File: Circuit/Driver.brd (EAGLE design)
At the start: 84.6 x 65.2 mm, 33 parts

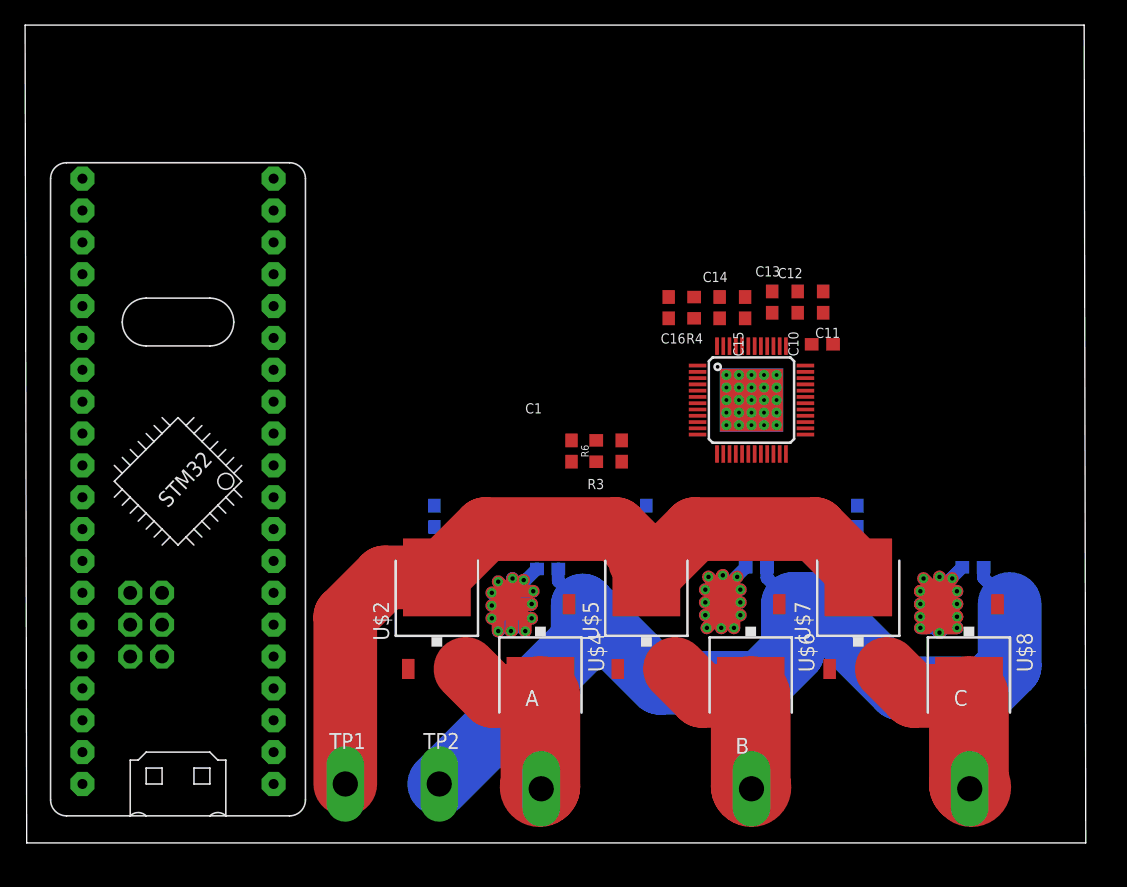
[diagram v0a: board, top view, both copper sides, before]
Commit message: enlarged the width of the vin and added a T-stop wire for large current signal (mosfet GND and VCC)
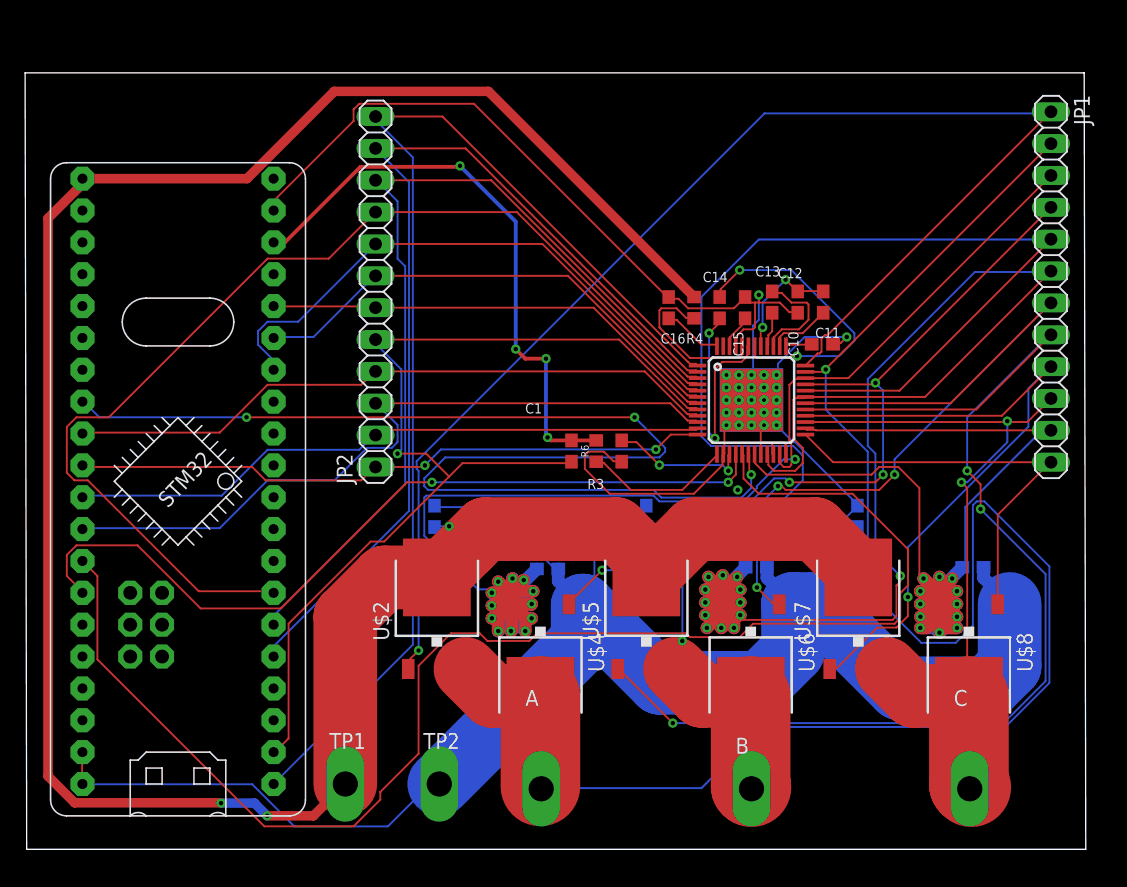
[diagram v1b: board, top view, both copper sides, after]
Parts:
- added JP1, JP2: (no value), pinhead:1X12
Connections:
- net GH_A: now also JP1.1
- net GH_B: now also JP1.8
- net GH_C: now also JP1.9
- net GL_A: now also JP1.4
- net GL_B: now also JP1.5
- net GL_C: now also JP1.12
- net PA10: now also JP2.9
- net PA4: now also JP2.4
- net PA5: now also JP2.1
- net PA6: now also JP2.2
- net PA7: now also JP2.3
- net PA8: now also JP2.11
- net PA9: now also JP2.10
- net PB12: now also JP2.12
- net PB13: now also JP2.5
- net PB6: now also JP2.8
- net PB7: now also JP2.7
- net PB8: now also JP2.6
- net SH_A: now also JP1.2
- net SH_B: now also JP1.7
- net SH_C: now also JP1.10
- net SN1: now also JP1.3
- net SN2: now also JP1.6
- net SN3: now also JP1.11
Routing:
- net GND: track 81.1 -> 288.9 mm, vias 0 -> 2
- net VIN: track 65.5 -> 199.6 mm, vias 0 -> 3
- net SH_A: track 14.2 -> 142.5 mm, vias 0 -> 1
- net PB0: track 0.00 -> 113.1 mm
- net GH_A: track 0.00 -> 107.6 mm, vias 0 -> 1
- net PA3: track 0.00 -> 98.5 mm, vias 0 -> 3
- net PB12: track 0.00 -> 92.9 mm
- net GH_B: track 0.00 -> 92.3 mm, vias 0 -> 3
- net GL_B: track 0.00 -> 88.6 mm, vias 0 -> 1
- net PA10: track 0.00 -> 87.2 mm
- net SN2: track 48.4 -> 133.1 mm, vias 12 -> 13
- net PB13: track 0.00 -> 81.7 mm, vias 0 -> 1
- net PA8: track 0.00 -> 79.2 mm
- net SN1: track 56.9 -> 134.9 mm, vias 12 -> 13
- net PA9: track 0.00 -> 73.0 mm
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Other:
- board size 84.6 x 65.2 mm -> 84.6 x 61.9 mm

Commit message: add a 5V pad input, delete the connection of Vin and Vbat, and add Description in Tname
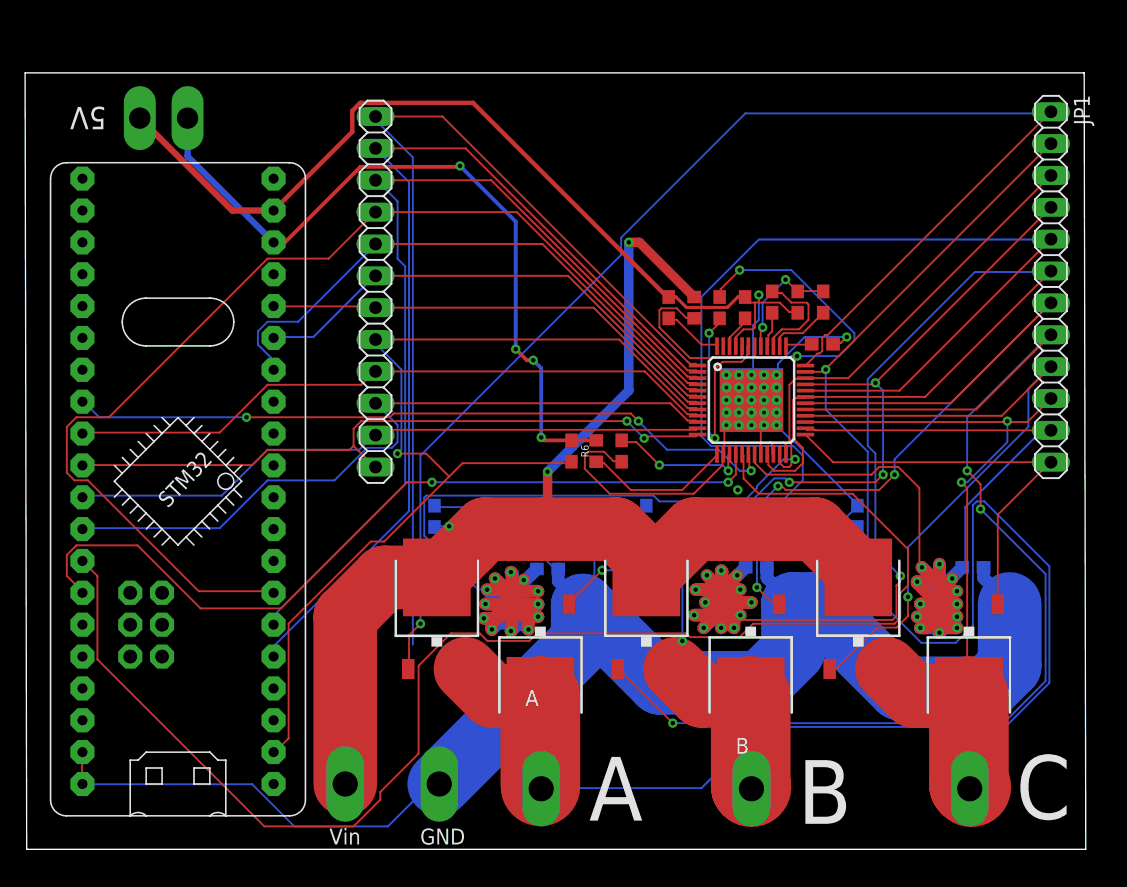
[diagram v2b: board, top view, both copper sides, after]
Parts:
- added 5V: TP2P2-38-17, testpad:P2-38-17
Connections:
- net GND: now also 5V.TP-1
- net VCC: now also 5V.TP-2
- net VIN: no longer U$1.P$40
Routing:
- net VIN: track 199.6 -> 99.0 mm
- net PA3: track 98.5 -> 57.3 mm
- net GND: track 288.9 -> 317.7 mm
- net PB12: track 92.9 -> 77.3 mm
- net VCC: track 46.9 -> 59.2 mm
- net SN1: track 134.9 -> 142.2 mm
- net SN2: track 133.1 -> 138.5 mm
- net SN3: track 108.2 -> 113.1 mm
- net PA5: track 51.0 -> 54.4 mm
- net GH_A: track 107.6 -> 108.4 mm
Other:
- board text added: "5V"
- board text added: "A"
- board text added: "B"
- board text added: "C"
- board text added: "GND"
- board text added: "Vin"

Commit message: fixed some bugs(Erc and Drc Errors)
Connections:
- removed net VIN1: C6.1
- removed net VIN2: C7.1
- removed net VREG: C16.1, U$3.48
- net VCC: now also C16.1, U$3.48
- net VIN: now also C6.1, C7.1
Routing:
- net VCC: track 59.2 -> 79.8 mm, vias 4 -> 7
- net PB12: track 77.3 -> 92.9 mm
- net VIN: track 99.0 -> 107.0 mm, vias 3 -> 5
- net VREG: track 4.87 -> 0.00 mm
- net GND: track 317.7 -> 318.3 mm

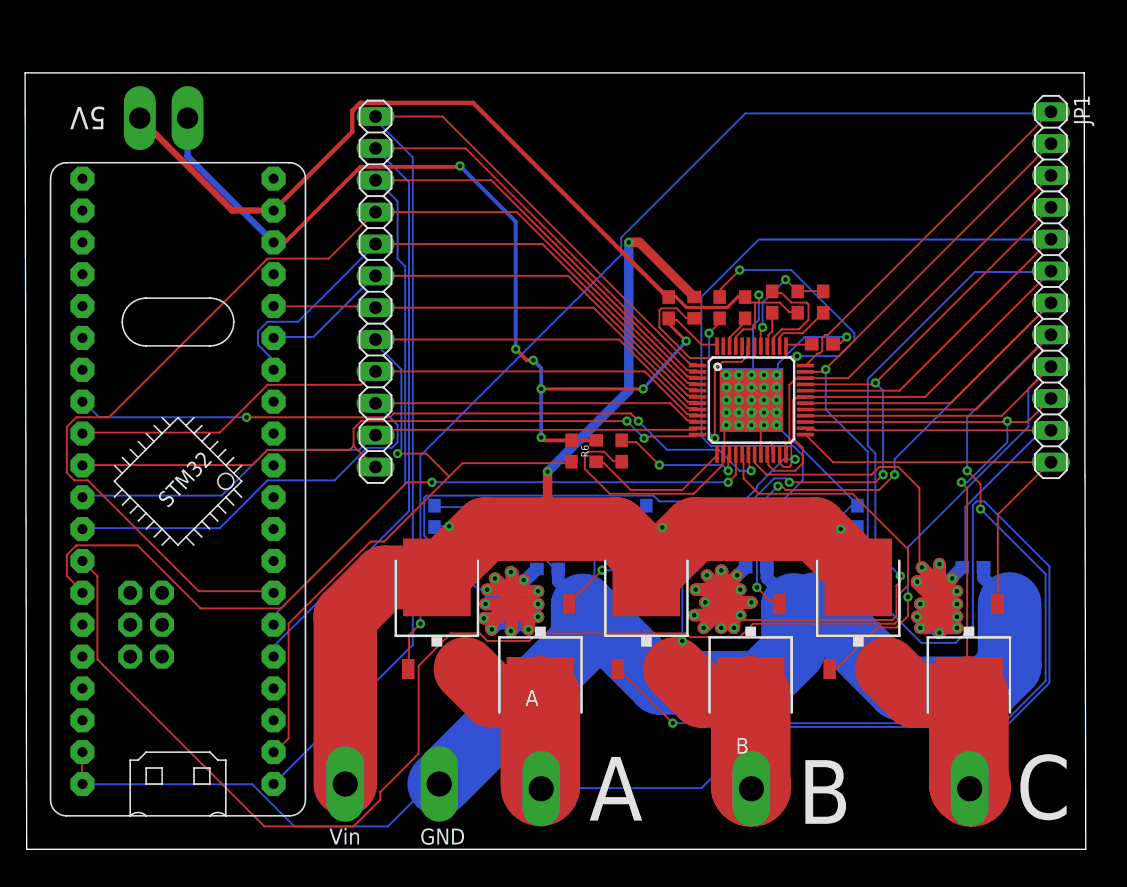
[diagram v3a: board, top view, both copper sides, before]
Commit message: Fixed the PVDD and VDrain pin's 'Vin' problem, Fixed some bugs
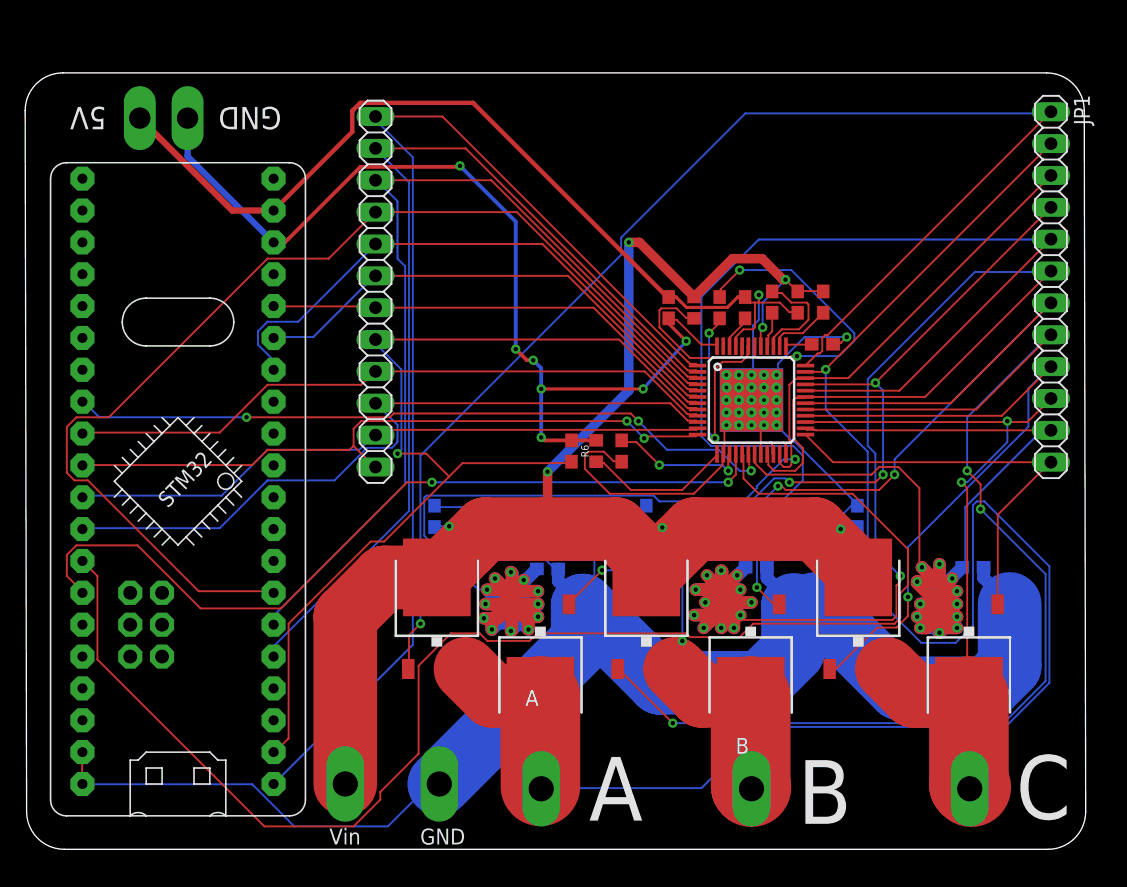
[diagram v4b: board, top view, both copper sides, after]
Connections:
- removed net PVDD: C11.1, C12.1, U$3.41
- net VIN: now also C11.1, C12.1, U$3.41
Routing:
- net VIN: track 107.0 -> 125.8 mm, vias 5 -> 7
- net PVDD: track 9.51 -> 0.00 mm, vias 2 -> 0
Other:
- board size 84.6 x 61.9 mm -> 84.5 x 61.9 mm
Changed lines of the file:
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@@
 <drawing>
 <settings>
-<setting alwaysvectorfont="no"/>
+<setting alwaysvectorfont="yes"/>
 <setting verticaltext="up"/>
 </settings>
-<grid distance="5" unitdist="mil" unit="mil" style="lines" multiple="1" display="yes" altdistance="5" altunitdist="mil" altunit="mil"/>
+<grid distance="25" unitdist="mil" unit="mil" style="lines" multiple="1" display="yes" altdistance="5" altunitdist="mil" altunit="mil"/>
 <layers>
 <layer number="1" name="Top" color="4" fill="1" visible="yes" active="yes"/>
@@
 <board>
 <plain>
-<wire x1="0" y1="-0.762" x2="84.435" y2="-0.762" width="0" layer="20"/>
-<wire x1="84.435" y1="-0.762" x2="84.308" y2="61.138" width="0" layer="20"/>
-<wire x1="84.308" y1="61.138" x2="-0.127" y2="61.138" width="0" layer="20"/>
-<wire x1="-0.127" y1="61.138" x2="0" y2="-0.762" width="0" layer="20"/>
+<wire x1="-0.12083125" y1="58.131340625" x2="-0.00614375" y2="2.232471875" width="0" layer="20"/>
+<wire x1="-0.00614375" y1="2.232471875" x2="2.99385" y2="-0.762" width="0" layer="20" curve="89.882424"/>
+<wire x1="2.99385" y1="-0.762" x2="81.4288375" y2="-0.762" width="0" layer="20"/>
+<wire x1="81.4288375" y1="-0.762" x2="84.42883125" y2="2.244659375" width="0" layer="20" curve="90.127185"/>
+<wire x1="84.42883125" y1="2.244659375" x2="84.31414375" y2="58.143528125" width="0" layer="20"/>
+<wire x1="84.31414375" y1="58.143528125" x2="81.31415" y2="61.138" width="0" layer="20" curve="89.882424"/>
+<wire x1="81.31415" y1="61.138" x2="2.8791625" y2="61.138" width="0" layer="20"/>
+<wire x1="2.8791625" y1="61.138" x2="-0.12083125" y2="58.131340625" width="0" layer="20" curve="90.127185"/>
 <wire x1="65.913" y1="21.717" x2="62.865" y2="24.765" width="5.08" layer="29"/>
 <wire x1="62.865" y1="24.765" x2="53.213" y2="24.765" width="5.08" layer="29"/>
@@
 <wire x1="75.184" y1="4.064" x2="75.184" y2="10.922" width="6.35" layer="29"/>
 <text x="6.35" y="58.42" size="1.778" layer="25" rot="SR180">5V</text>
-<text x="19.685" y="58.42" size="1.778" layer="26" rot="SR180">GND</text>
 <text x="24.13" y="-0.381" size="1.27" layer="25">Vin</text>
 <text x="31.369" y="-0.381" size="1.27" layer="25">GND</text>
@@
 <text x="61.468" y="1.27" size="5.08" layer="21">B</text>
 <text x="78.867" y="1.651" size="5.08" layer="21">C</text>
+<wire x1="38.735" y1="19.05" x2="38.608" y2="18.923" width="5.588" layer="29"/>
+<wire x1="38.608" y1="18.923" x2="38.608" y2="18.669" width="5.588" layer="29"/>
+<wire x1="55.245" y1="18.923" x2="55.245" y2="19.304" width="5.08" layer="29"/>
+<wire x1="72.39" y1="21.209" x2="72.771" y2="20.828" width="3.81" layer="29"/>
+<wire x1="72.771" y1="20.828" x2="72.771" y2="18.161" width="3.81" layer="29"/>
+<wire x1="71.247" y1="18.923" x2="71.247" y2="18.034" width="0.762" layer="29"/>
+<wire x1="71.247" y1="18.034" x2="70.993" y2="17.78" width="0.762" layer="29"/>
+<wire x1="70.993" y1="17.78" x2="70.993" y2="17.145" width="0.762" layer="29"/>
+<wire x1="70.993" y1="17.145" x2="71.628" y2="16.51" width="0.762" layer="29"/>
+<wire x1="71.628" y1="16.51" x2="72.771" y2="16.51" width="0.762" layer="29"/>
+<wire x1="57.785" y1="18.923" x2="54.102" y2="18.923" width="0.762" layer="29"/>
+<wire x1="38.354" y1="18.923" x2="38.608" y2="18.669" width="0.762" layer="30"/>
+<wire x1="38.608" y1="18.669" x2="38.608" y2="18.542" width="0.762" layer="30"/>
+<wire x1="55.753" y1="18.923" x2="55.626" y2="18.923" width="6.35" layer="30"/>
+<wire x1="70.993" y1="20.574" x2="72.771" y2="18.796" width="1.016" layer="30"/>
+<wire x1="72.771" y1="18.796" x2="74.168" y2="18.796" width="1.016" layer="30"/>
+<wire x1="74.168" y1="18.796" x2="74.168" y2="19.812" width="1.016" layer="30"/>
+<wire x1="74.168" y1="19.812" x2="73.787" y2="20.193" width="1.016" layer="30"/>
+<wire x1="73.787" y1="20.193" x2="73.787" y2="20.828" width="1.016" layer="30"/>
+<wire x1="73.787" y1="20.828" x2="72.771" y2="21.844" width="1.016" layer="30"/>
+<wire x1="72.771" y1="21.844" x2="72.771" y2="21.971" width="1.016" layer="30"/>
+<wire x1="72.771" y1="21.971" x2="71.628" y2="21.971" width="1.016" layer="30"/>
+<wire x1="71.628" y1="21.971" x2="70.993" y2="21.336" width="1.016" layer="30"/>
+<wire x1="70.993" y1="21.336" x2="70.993" y2="20.574" width="1.016" layer="30"/>
+<wire x1="70.993" y1="20.574" x2="71.628" y2="20.574" width="1.016" layer="30"/>
+<wire x1="71.628" y1="20.574" x2="72.136" y2="21.082" width="1.016" layer="30"/>
+<wire x1="72.136" y1="21.082" x2="72.136" y2="20.955" width="1.016" layer="30"/>
+<wire x1="72.136" y1="20.955" x2="72.644" y2="20.447" width="1.016" layer="30"/>
+<wire x1="73.406" y1="19.685" x2="72.644" y2="20.447" width="1.016" layer="30"/>
+<wire x1="72.644" y1="20.447" x2="72.009" y2="20.447" width="1.016" layer="30"/>
+<wire x1="72.009" y1="20.447" x2="72.009" y2="19.558" width="1.016" layer="30"/>
+<wire x1="72.009" y1="19.558" x2="70.993" y2="18.542" width="1.016" layer="30"/>
+<wire x1="70.993" y1="18.542" x2="70.993" y2="17.78" width="1.016" layer="30"/>
+<wire x1="70.993" y1="17.78" x2="70.993" y2="17.145" width="1.016" layer="30"/>
+<wire x1="70.993" y1="17.145" x2="71.247" y2="16.891" width="1.016" layer="30"/>
+<wire x1="71.247" y1="16.891" x2="71.628" y2="16.51" width="1.016" layer="30"/>
+<wire x1="71.628" y1="16.51" x2="73.787" y2="16.51" width="1.016" layer="30"/>
+<wire x1="73.787" y1="16.51" x2="74.168" y2="16.891" width="1.016" layer="30"/>
+<wire x1="74.168" y1="16.891" x2="74.168" y2="17.018" width="1.016" layer="30"/>
+<wire x1="74.168" y1="17.78" x2="74.168" y2="18.796" width="1.016" layer="30"/>
+<wire x1="74.168" y1="19.812" x2="73.025" y2="19.812" width="1.016" layer="30"/>
+<wire x1="73.025" y1="19.812" x2="70.993" y2="17.78" width="1.016" layer="30"/>
+<wire x1="70.993" y1="17.78" x2="74.168" y2="17.78" width="1.016" layer="30"/>
+<wire x1="74.168" y1="17.78" x2="74.168" y2="17.018" width="1.016" layer="30"/>
+<wire x1="74.168" y1="17.018" x2="74.041" y2="16.891" width="1.016" layer="30"/>
+<wire x1="74.041" y1="16.891" x2="71.247" y2="16.891" width="1.016" layer="30"/>
+<wire x1="38.608" y1="18.923" x2="38.608" y2="18.669" width="5.842" layer="30"/>
+<text x="20.32" y="58.42" size="1.778" layer="25" rot="SR180">GND</text>
 </plain>
 <attributes>
@@
 <wire x1="50.7492" y1="24.9936" x2="52.1154" y2="23.6274" width="0.1524" layer="1"/>
 <wire x1="50.7492" y1="24.9936" x2="50.673" y2="24.892" width="0.1524" layer="1"/>
+<contactref element="C11" pad="1"/>
+<contactref element="U$3" pad="41"/>
+<contactref element="C12" pad="1"/>
+<wire x1="63.3984" y1="43.7388" x2="61.5696" y2="43.7388" width="0.1524" layer="1"/>
+<wire x1="61.5696" y1="43.7388" x2="61.468" y2="43.7125" width="0.1524" layer="1"/>
+<wire x1="63.3984" y1="43.7388" x2="63.5" y2="43.7125" width="0.1524" layer="1"/>
+<wire x1="58.5216" y1="40.6908" x2="58.5216" y2="39.4716" width="0.1524" layer="1"/>
+<wire x1="58.674" y1="40.8432" x2="58.5216" y2="40.6908" width="0.1524" layer="1"/>
+<wire x1="58.674" y1="42.8244" x2="58.674" y2="40.8432" width="0.1524" layer="16"/>
+<wire x1="60.5028" y1="44.6532" x2="58.674" y2="42.8244" width="0.1524" layer="16"/>
+<wire x1="61.4172" y1="43.7388" x2="60.5028" y2="44.6532" width="0.1524" layer="1"/>
+<wire x1="58.5216" y1="39.4716" x2="58.535" y2="39.352" width="0.1524" layer="1"/>
+<wire x1="61.4172" y1="43.7388" x2="61.468" y2="43.7125" width="0.1524" layer="1"/>
+<via x="58.674" y="40.8432" extent="1-16" drill="0.35"/>
+<via x="60.5028" y="44.6532" extent="1-16" drill="0.35"/>
+<wire x1="60.29964375" y1="44.6532" x2="60.5028" y2="44.6532" width="0.762" layer="1"/>
+<wire x1="53.213" y1="43.268" x2="56.2718" y2="46.3268" width="0.762" layer="1"/>
+<wire x1="56.2718" y1="46.3268" x2="58.62604375" y2="46.3268" width="0.762" layer="1"/>
+<wire x1="58.62604375" y1="46.3268" x2="60.29964375" y2="44.6532" width="0.762" layer="1"/>
 </signal>
 <signal name="PB12">
@@
 <via x="61.2648" y="30.3276" extent="1-16" drill="0.35"/>
 </signal>
-<signal name="PVDD">
-<contactref element="C11" pad="1"/>
-<contactref element="U$3" pad="41"/>
-<contactref element="C12" pad="1"/>
-<wire x1="63.3984" y1="43.7388" x2="61.5696" y2="43.7388" width="0.1524" layer="1"/>
-<wire x1="61.5696" y1="43.7388" x2="61.468" y2="43.7125" width="0.1524" layer="1"/>
-<wire x1="63.3984" y1="43.7388" x2="63.5" y2="43.7125" width="0.1524" layer="1"/>
-<wire x1="58.5216" y1="40.6908" x2="58.5216" y2="39.4716" width="0.1524" layer="1"/>
-<wire x1="58.674" y1="40.8432" x2="58.5216" y2="40.6908" width="0.1524" layer="1"/>
-<wire x1="58.674" y1="42.8244" x2="58.674" y2="40.8432" width="0.1524" layer="16"/>
-<wire x1="60.5028" y1="44.6532" x2="58.674" y2="42.8244" width="0.1524" layer="16"/>
-<wire x1="61.4172" y1="43.7388" x2="60.5028" y2="44.6532" width="0.1524" layer="1"/>
-<wire x1="58.5216" y1="39.4716" x2="58.535" y2="39.352" width="0.1524" layer="1"/>
-<wire x1="61.4172" y1="43.7388" x2="61.468" y2="43.7125" width="0.1524" layer="1"/>
-<via x="58.674" y="40.8432" extent="1-16" drill="0.35"/>
-<via x="60.5028" y="44.6532" extent="1-16" drill="0.35"/>
-</signal>
 <signal name="PWRGD">
